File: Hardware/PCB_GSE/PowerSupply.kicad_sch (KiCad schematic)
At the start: 56 parts, among them J2 Vin_XT30PW-F, U2 LM2673SX-12_NOPB, U3 MPQ9843GLE-5-AEC1-Z, U4 TLV75733PDBVR

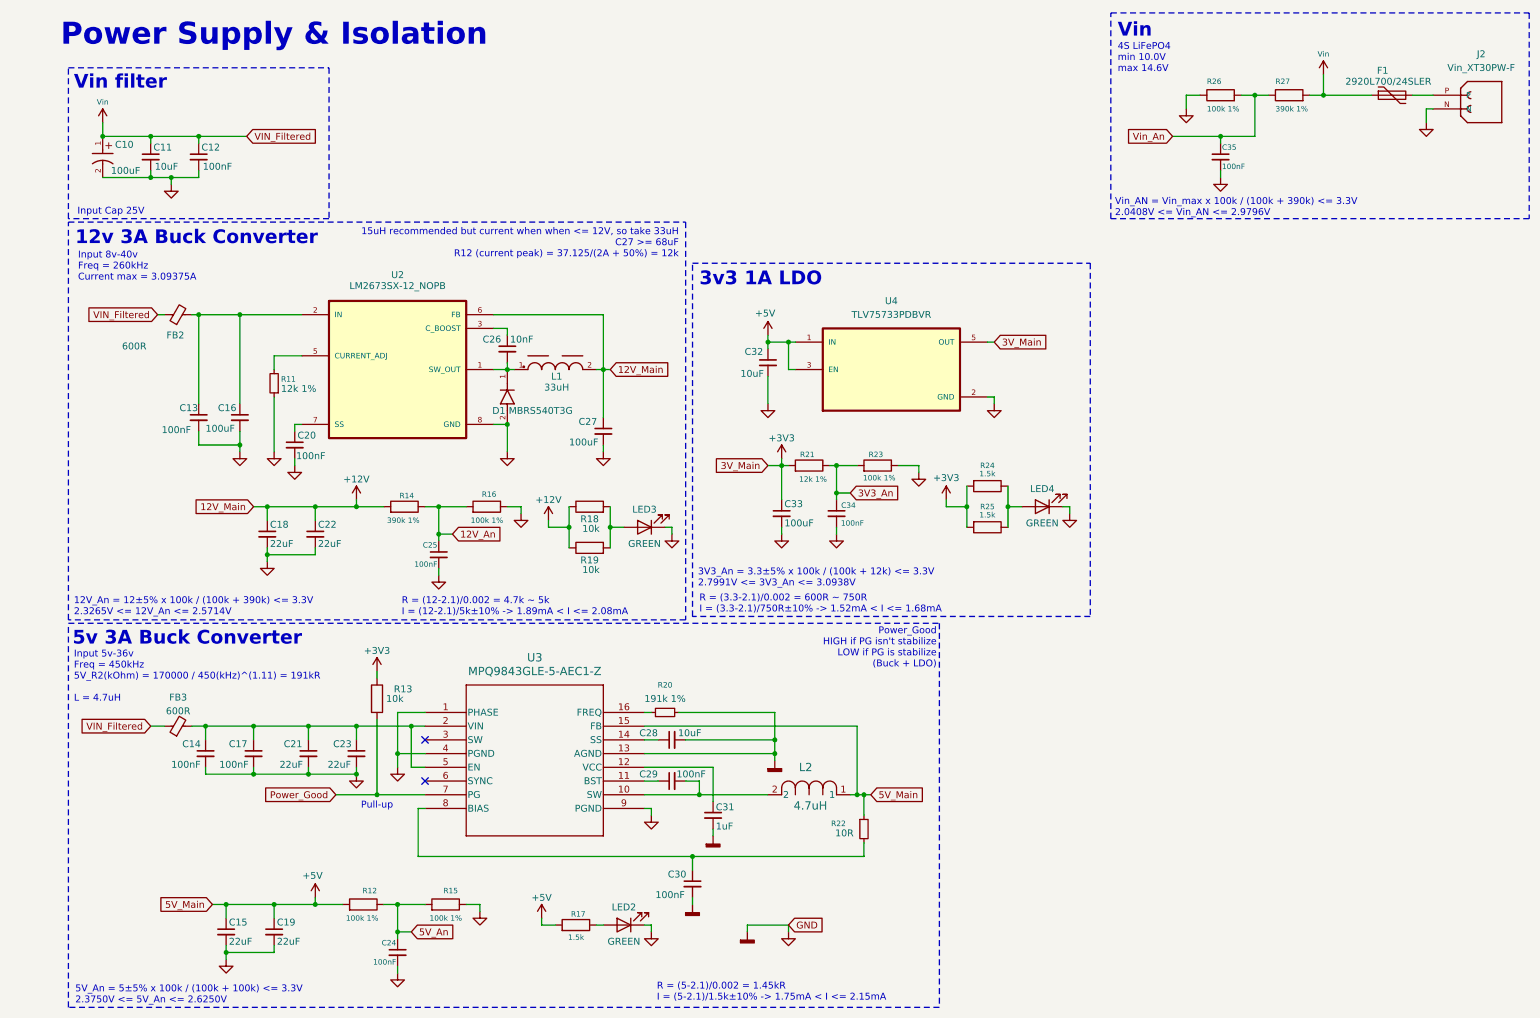
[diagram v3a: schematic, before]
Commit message: chore: Change buck 12v
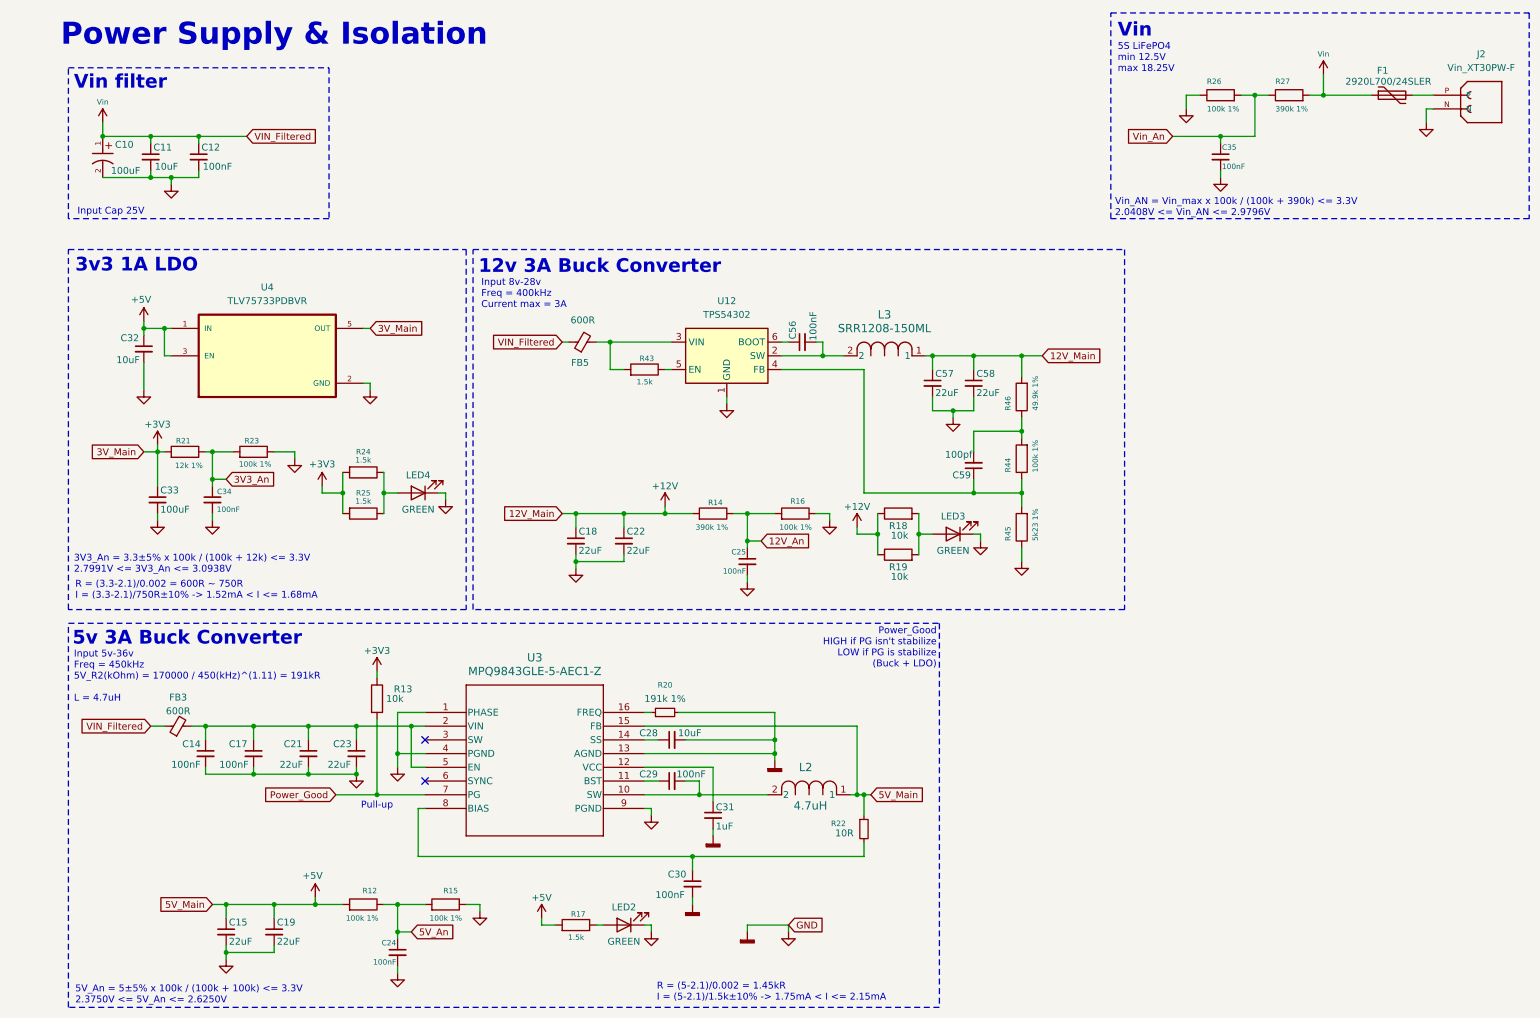
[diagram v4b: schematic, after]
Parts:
- removed C13, C20: 100nF, Capacitor_SMD:C_0603_1608Metric, symbol Device:C_Small
- removed C16, C27: 100uF, Capacitor_SMD:C_1210_3225Metric, symbol Device:C_Small
- removed C26: 10nF, Capacitor_SMD:C_0805_2012Metric, symbol Device:C_Small
- removed D1: MBRS540T3G, pcb_moteur:DIODE_SMB_2L_ONS, symbol PCB_GSE:MBRS540T3G
- removed FB2: 600R, Inductor_SMD:L_1210_3225Metric, symbol Device:FerriteBead_Small
- removed L1: 33uH, pcb_moteur:WE-PD_1245, symbol PCB_GSE:WE-PD_1245
- removed R11: 12k 1%, Resistor_SMD:R_0805_2012Metric, symbol Device:R_Small
- removed U2: LM2673SX-12_NOPB, PCB_GSE:LM2673SX-12_NOPB, symbol PCB_GSE:LM2673SX-12_NOPB
- added C56: 100nF, Capacitor_SMD:C_0603_1608Metric, symbol Device:C_Small
- added C57, C58: 22uF, Capacitor_SMD:C_0805_2012Metric, symbol Device:C_Small
- added C59: 100pf, Capacitor_SMD:C_0603_1608Metric, symbol Device:C_Small
- added FB5: 600R, Inductor_SMD:L_1210_3225Metric, symbol Device:FerriteBead_Small
- added L3: SRR1208-150ML, PCB_GSE:IND_BOURNS_SRR1208, symbol PCB_GSE:SRR1208-150ML
- added R43: 1.5k, Resistor_SMD:R_0805_2012Metric, symbol Device:R
- added R44: 100k 1%, Resistor_SMD:R_0805_2012Metric, symbol Device:R
- added R45: 5k23 1%, Resistor_SMD:R_0603_1608Metric, symbol Device:R
- added R46: 49.9k 1%, Resistor_SMD:R_0603_1608Metric, symbol Device:R
- added U12: TPS54302, Package_TO_SOT_SMD:SOT-23-6, symbol Regulator_Switching:TPS54302
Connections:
- net +12V: now also C57.1, C58.1, L3.1, R46.2
- net AGND5V: now also C57.2, C58.2, R45.1, U12.1 (GND)
- net Vin: now also FB5.1
- new net: C56.1, U12.6 (BOOT)
- new net: C56.2, L3.2, U12.2 (SW)
- new net: FB5.2, R43.2, U12.3 (VIN)
- new net: C59.1, R44.1, R45.2, U12.4 (FB)
- new net: C59.2, R44.2, R46.1
- new net: R43.1, U12.5 (EN)
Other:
- note added: "5S LiFePO4 min 12.5V max 18.25V"
- note added: "Input 8v-28v Freq = 400kHz Current max = 3A"
- note removed: "12V_An = 12±5% x 100k / (100k + 390k) <= 3.3V 2.3265V <= 12V_An <= 2.5714V"
- note removed: "15uH recommended but current when when <= 12V, so take 33uH C27 >= 68uF R12 (current peak) = 37.125/(2A + 50%) = 12k"
- note removed: "4S LiFePO4 min 10.0V max 14.6V"
- note removed: "Input 8v-40v Freq = 260kHz Current max = 3.09375A"
- note removed: "R = (12-2.1)/0.002 = 4.7k ~ 5k I = (12-2.1)/5k±10% -> 1.89mA < I <= 2.08mA"
- moved on the sheet: C18, C22, C25, C32, C33, C34, LED3, LED4, R14, R16, R18, R19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

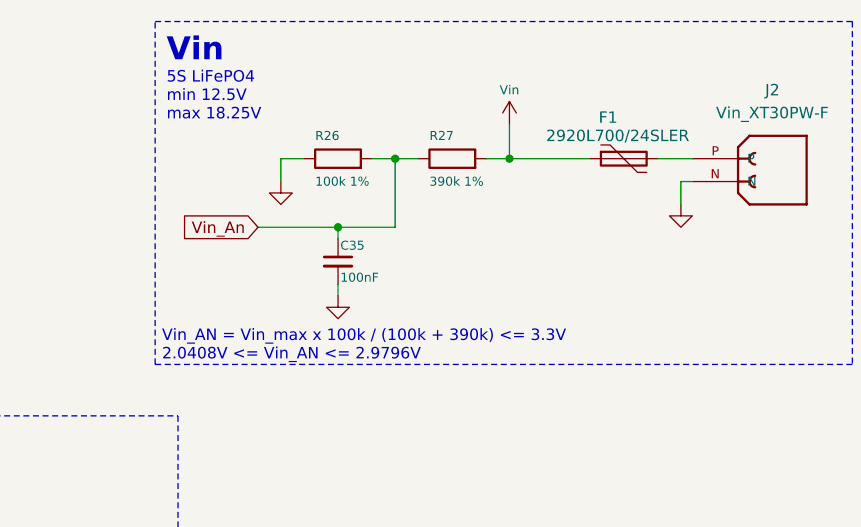
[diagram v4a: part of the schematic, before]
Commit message: fix(GSE & Moteur): change Vin adc divider
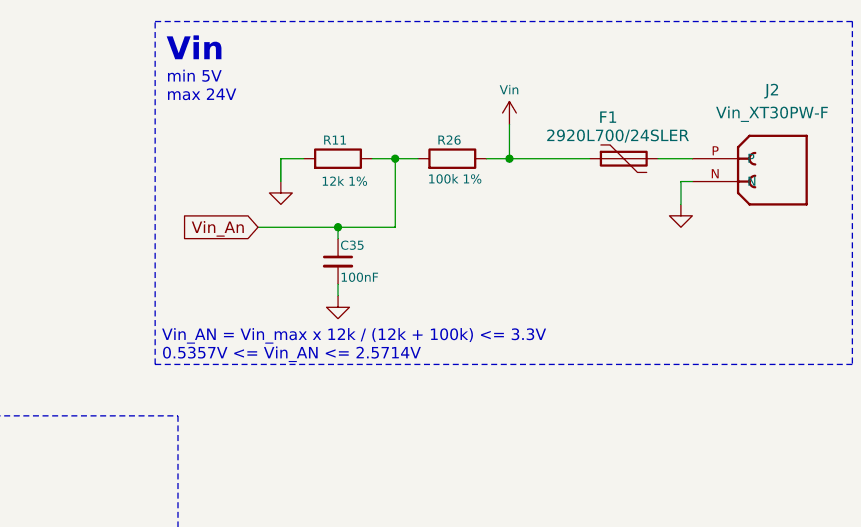
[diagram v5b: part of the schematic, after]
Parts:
- removed R27: 390k 1%, Resistor_SMD:R_0805_2012Metric, symbol Device:R
- added R11: 12k 1%, Resistor_SMD:R_0805_2012Metric, symbol Device:R
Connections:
- net AGND5V: now also R11.2; no longer R26.1
- net Vin: now also R26.1
- net Vin_An: now also R11.1
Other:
- note added: "Vin_AN = Vin_max x 12k / (12k + 100k) <= 3.3V 0.5357V <= Vin_AN <= 2.5714V"
- note added: "min 5V max 24V"
- note removed: "5S LiFePO4 min 12.5V max 18.25V"
- note removed: "Vin_AN = Vin_max x 100k / (100k + 390k) <= 3.3V 2.0408V <= Vin_AN <= 2.9796V"

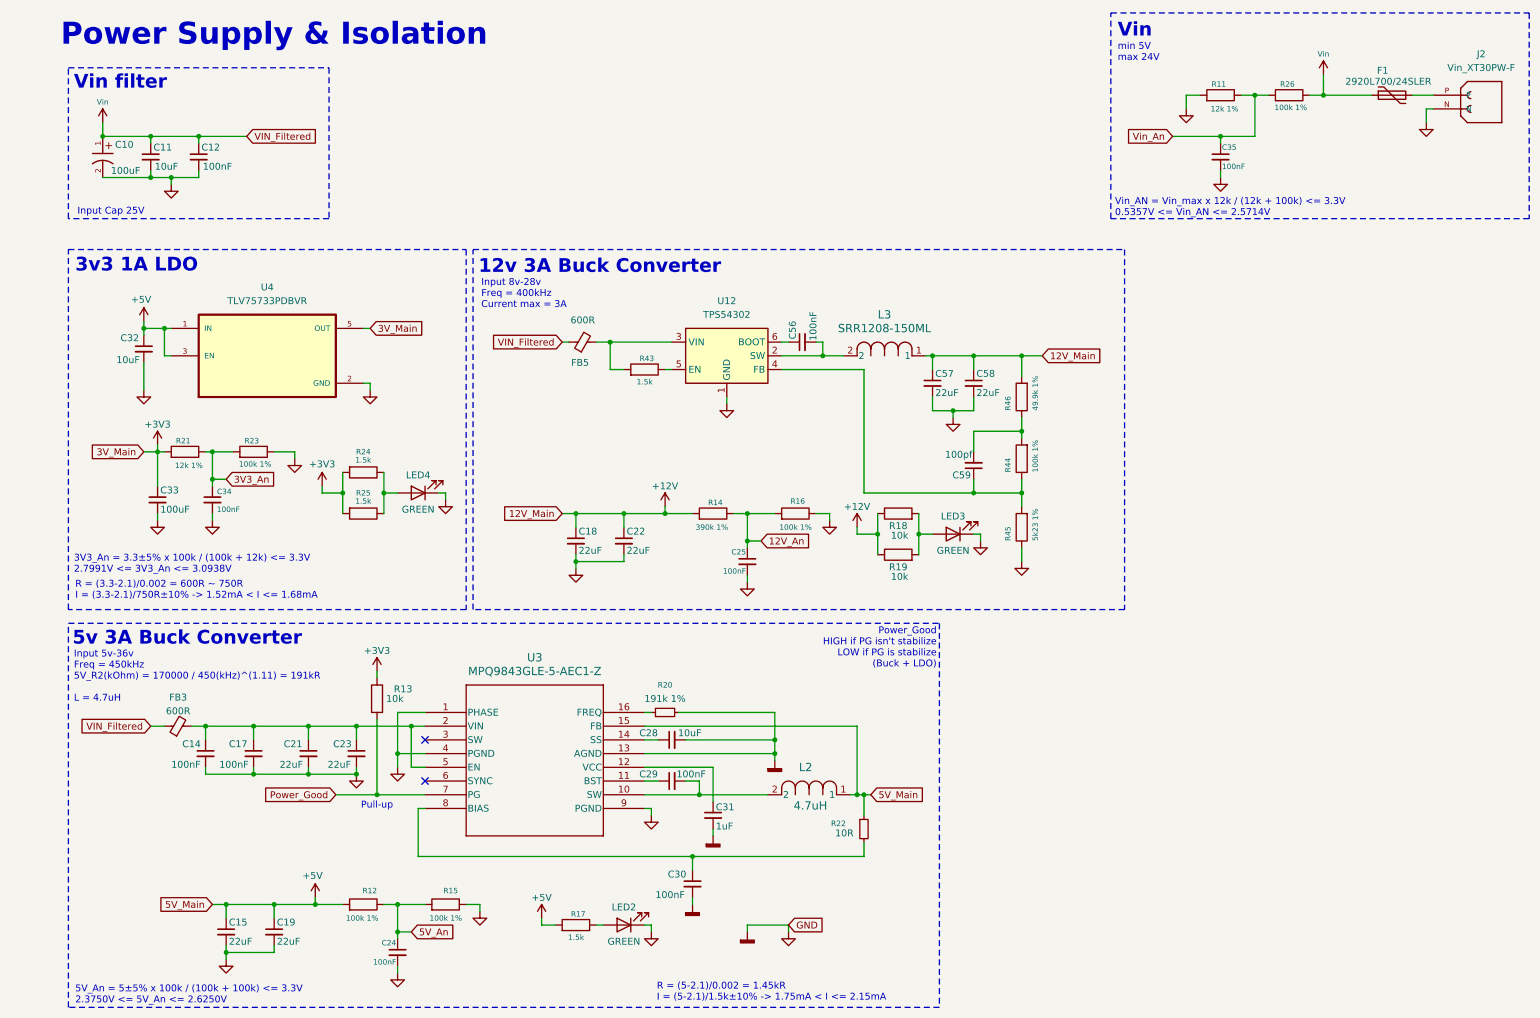
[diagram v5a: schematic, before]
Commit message: change 12V buck to 12V buck-boost
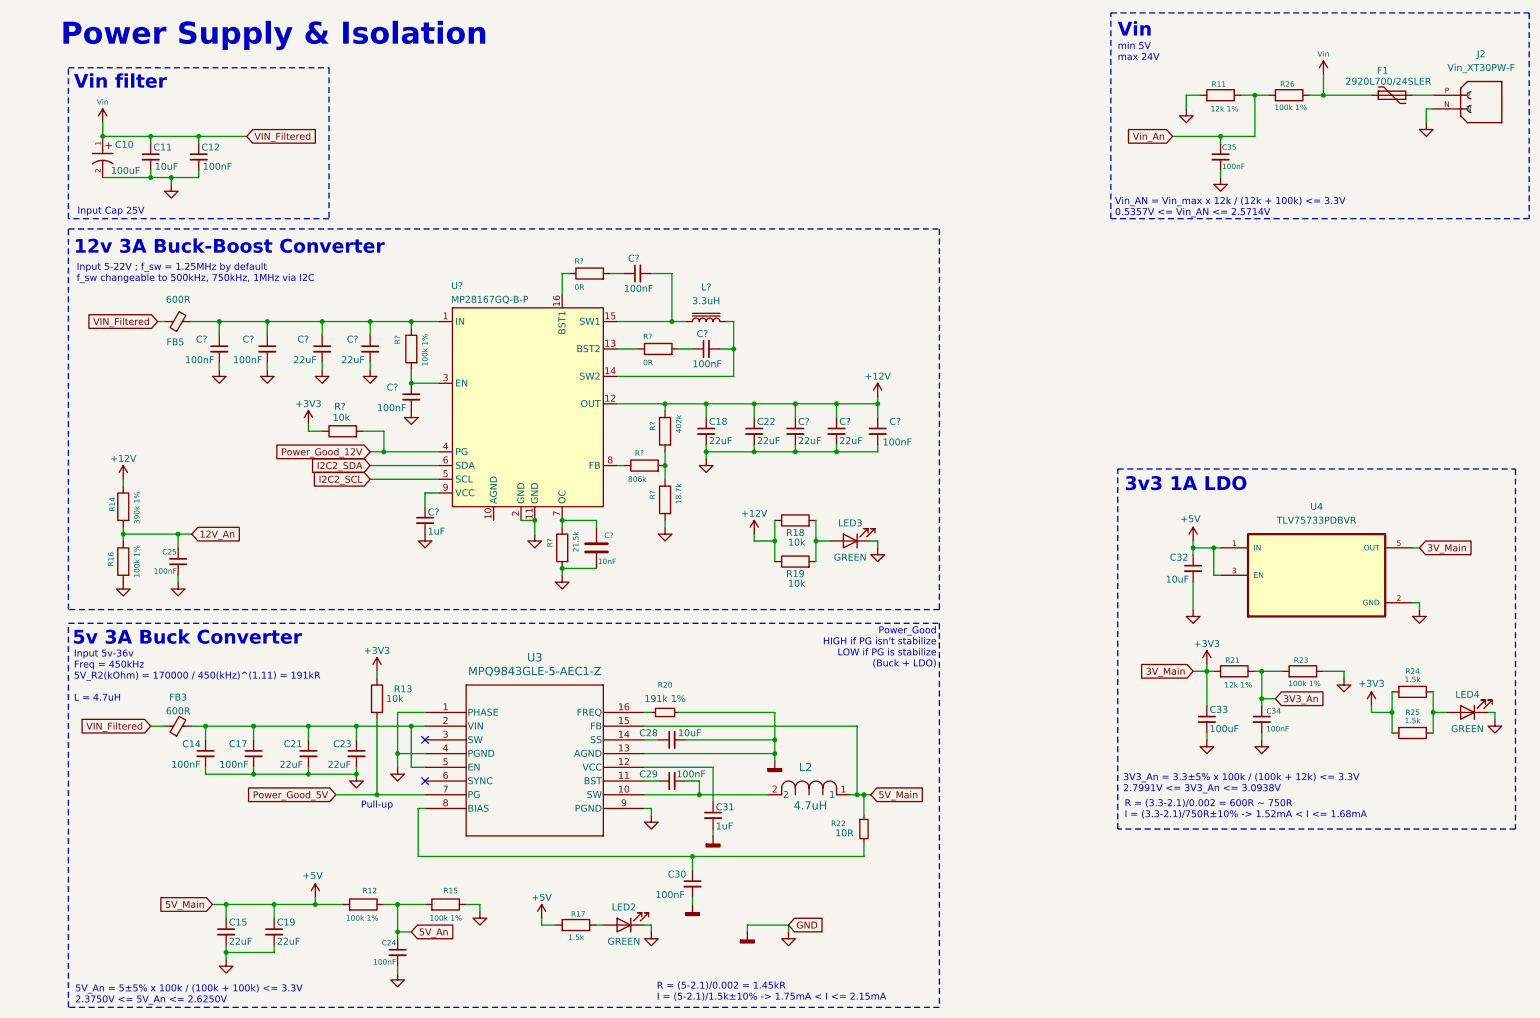
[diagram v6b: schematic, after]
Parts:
- removed C56: 100nF, Capacitor_SMD:C_0603_1608Metric, symbol Device:C_Small
- removed C57, C58: 22uF, Capacitor_SMD:C_0805_2012Metric, symbol Device:C_Small
- removed C59: 100pf, Capacitor_SMD:C_0603_1608Metric, symbol Device:C_Small
- removed L3: SRR1208-150ML, PCB_GSE:IND_BOURNS_SRR1208, symbol PCB_GSE:SRR1208-150ML
- removed R43: 1.5k, Resistor_SMD:R_0805_2012Metric, symbol Device:R
- removed R44: 100k 1%, Resistor_SMD:R_0805_2012Metric, symbol Device:R
- removed R45: 5k23 1%, Resistor_SMD:R_0603_1608Metric, symbol Device:R
- removed R46: 49.9k 1%, Resistor_SMD:R_0603_1608Metric, symbol Device:R
- removed U12: TPS54302, Package_TO_SOT_SMD:SOT-23-6, symbol Regulator_Switching:TPS54302
- added C? (x4): 22uF, Capacitor_SMD:C_0805_2012Metric, symbol Device:C_Small
- added C? (x6): 100nF, Capacitor_SMD:C_0603_1608Metric, symbol Device:C_Small
- added C?: 10nF, Capacitor_SMD:C_0805_2012Metric, symbol Device:C
- added C?: 1uF, Capacitor_SMD:C_0805_2012Metric, symbol Device:C_Small
- added L?: 3.3uH, PCB_GSE:MPL-AL6050-3R3, symbol Device:L_Iron
- added R?: 21.5k, Resistor_SMD:R_0805_2012Metric, symbol Device:R
- added R?: 806k, Resistor_SMD:R_0805_2012Metric, symbol Device:R
- added R? (x2): 0R, Resistor_SMD:R_0805_2012Metric, symbol Device:R
- added R?: 402k, Resistor_SMD:R_0805_2012Metric, symbol Device:R
- added R?: 100k 1%, Resistor_SMD:R_0805_2012Metric, symbol Device:R
- added R?: 18.7k, Resistor_SMD:R_0805_2012Metric, symbol Device:R
- added R?: 10k, Resistor_SMD:R_0805_2012Metric, symbol Device:R
- added U?: MP28167GQ-B-P, PCB_GSE:QFN-16_MP28167_MNP, symbol PCB_GSE:MP28167-B
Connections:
- net +12V: now also R14.1, C?.1, C?.1, C?.1, R?.1, U?.12 (OUT); no longer R14.2
- net +3V3: now also R?.1
- net 12V_An: now also R14.2, R16.1; no longer R14.1, R16.2
- net AGND5V: now also R16.2, C?.1, C?.2, C?.2, C?.2, C?.2, C?.2, C?.2, C?.2, C?.2, C?.2, R?.2, R?.2, U?.11 (GND), U?.2 (GND); no longer R16.1
- net at FB5.2: now also C?.1, C?.1, C?.1, C?.1, R?.1, U?.1 (IN)
- net Power_Good renamed Power_Good_5V
- new net: C?.2, R?.1, U?.7 (OC)
- new net: R?.1, U?.8 (FB)
- new net: R?.1, R?.2, R?.2
- new net: R?.1, U?.16 (BST1)
- new net: C?.1, R?.2 (x2)
- new net: C?.2, L?.1, U?.15 (SW1)
- new net: C?.2, L?.2, U?.14 (SW2)
- new net: C?.1, R?.2, U?.3 (EN)
- new net: R?.1, U?.13 (BST2)
- new net: C?.1, U?.9 (VCC)
- new net I2C2_SCL: U?.5 (SCL)
- new net I2C2_SDA: U?.6 (SDA)
- new net Power_Good_12V: R?.2, U?.4 (PG)
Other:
- note added: "12v 3A Buck-Boost Converter"
- note added: "Input 5-22V ; f_sw = 1.25MHz by default f_sw changeable to 500kHz, 750kHz, 1MHz via I2C"
- note removed: "12v 3A Buck Converter"
- note removed: "Input 8v-28v Freq = 400kHz Current max = 3A"
- moved on the sheet: C18, C22, C25, C32, C33, C34, FB5, LED3, LED4, R14, R16, R18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
